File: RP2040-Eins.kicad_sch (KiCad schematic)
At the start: 55 parts, among them J1 Barrel_Jack_Switch, J10 USB_C_Receptacle_USB2.0, J2 CONN_I, J3 CONN_A, J4 CONN_P, J5 CONN_X, J7 CONN_JTAG, J8 CONN_D1, J9 CONN_D2, Q1 AO3401A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

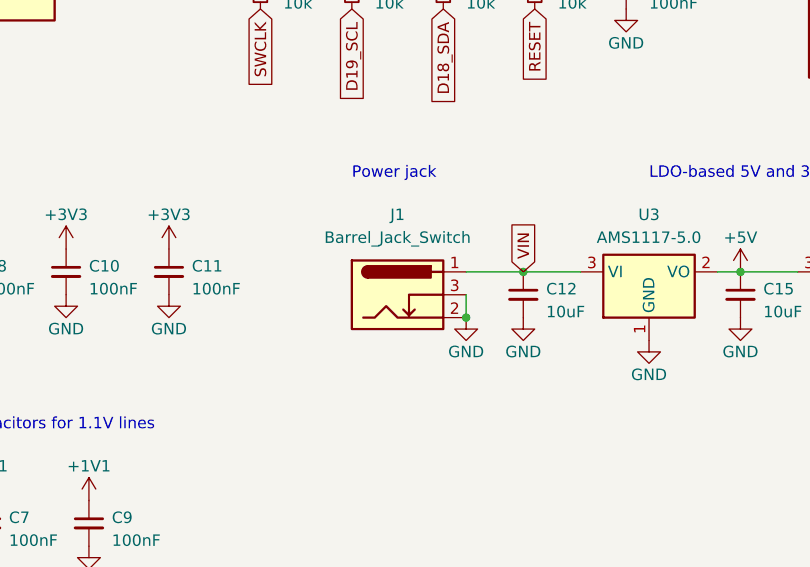
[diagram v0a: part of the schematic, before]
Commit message: Added polarity reversion protection diode
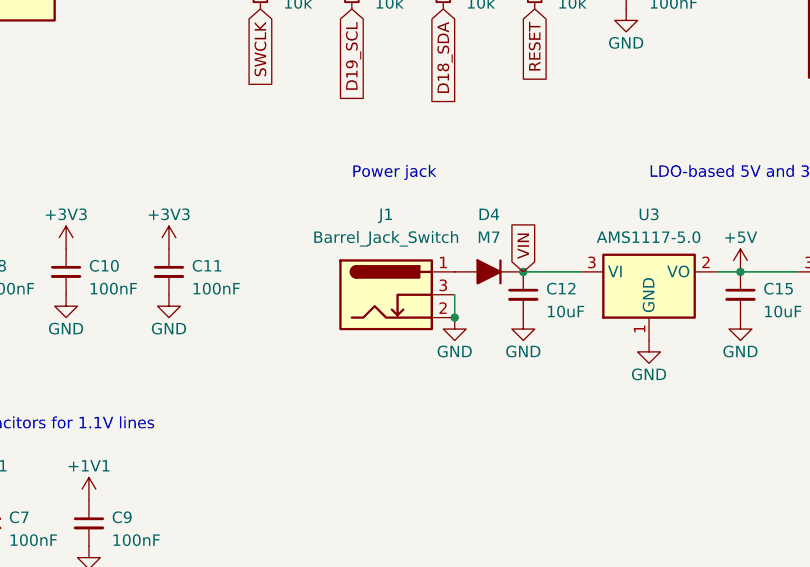
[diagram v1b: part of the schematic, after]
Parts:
- added D4: M7, PCM_4ms_Diode:D_DO-214AC_SMA, symbol PCM_Diode_AKL:M7
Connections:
- net VIN: now also D4.1 (K); no longer J1.1
- new net: D4.2 (A), J1.1
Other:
- moved on the sheet: J1
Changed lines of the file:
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@@
   (junction (at 262.89 146.05) (diameter 0) (color 0 0 0 0)
   )
+  (junction (at 207.01 151.13) (diameter 0) (color 0 0 0 0)
+  )
   (junction (at 86.36 177.8) (diameter 0) (color 0 0 0 0)
   )
@@
   (junction (at 90.17 92.71) (diameter 0) (color 0 0 0 0)
   )
-  (junction (at 208.28 151.13) (diameter 0) (color 0 0 0 0)
-  )
   (junction (at 135.89 30.48) (diameter 0) (color 0 0 0 0)
   )
@@
   (junction (at 238.76 146.05) (diameter 0) (color 0 0 0 0)
   )
-  (junction (at 49.53 96.52) (diameter 0) (color 0 0 0 0)
-  )
   (junction (at 214.63 146.05) (diameter 0) (color 0 0 0 0)
   )
+  (junction (at 49.53 96.52) (diameter 0) (color 0 0 0 0)
+  )
   (junction (at 256.54 127) (diameter 0) (color 0 0 0 0)
   )
@@
     (stroke (width 0) (type default))
   )
-  (wire (pts (xy 208.28 146.05) (xy 214.63 146.05))
-    (stroke (width 0) (type default))
-  )
   (wire (pts (xy 80.01 66.04) (xy 80.01 71.12))
     (stroke (width 0) (type default))
@@
     (stroke (width 0) (type default))
   )
+  (wire (pts (xy 207.01 148.59) (xy 207.01 151.13))
+    (stroke (width 0) (type default))
+  )
   (wire (pts (xy 143.51 30.48) (xy 146.05 30.48))
     (stroke (width 0) (type default))
@@
     (stroke (width 0) (type default))
   )
-  (wire (pts (xy 208.28 148.59) (xy 208.28 151.13))
-    (stroke (width 0) (type default))
-  )
   (wire (pts (xy 90.17 68.58) (xy 90.17 71.12))
     (stroke (width 0) (type default))
@@
     )
   )
-  (symbol (lib_id "power:GND") (at 208.28 151.13 0) (unit 1)
+  (symbol (lib_id "power:GND") (at 207.01 151.13 0) (unit 1)
     (in_bom yes) (on_board yes) (dnp no)
-    (property "Reference" "#PWR058" (at 208.28 157.48 0)
+    (property "Reference" "#PWR058" (at 207.01 157.48 0)
       (effects (font (size 1.27 1.27)) hide)
     )
-    (property "Value" "GND" (at 208.28 154.94 0)
+    (property "Value" "GND" (at 207.01 154.94 0)
       (effects (font (size 1.27 1.27)))
     )
-    (property "Footprint" "" (at 208.28 151.13 0)
+    (property "Footprint" "" (at 207.01 151.13 0)
       (effects (font (size 1.27 1.27)) hide)
     )
-    (property "Datasheet" "" (at 208.28 151.13 0)
+    (property "Datasheet" "" (at 207.01 151.13 0)
       (effects (font (size 1.27 1.27)) hide)
     )
@@
     )
   )
+  (symbol (lib_id "PCM_Diode_AKL:M7") (at 210.82 146.05 0) (unit 1)
+    (in_bom yes) (on_board yes) (dnp no) (fields_autoplaced)
+    (property "Reference" "D4" (at 210.82 139.7 0)
+      (effects (font (size 1.27 1.27)))
+    )
+    (property "Value" "M7" (at 210.82 142.24 0)
+      (effects (font (size 1.27 1.27)))
+    )
+    (property "Footprint" "PCM_4ms_Diode:D_DO-214AC_SMA" (at 210.82 146.05 0)
+      (effects (font (size 1.27 1.27)) hide)
+    )
+    (property "Datasheet" "https://www.tme.eu/Document/0550e9bf27627c5cdfb653945cb570ca/m1-m7.pdf" (at 210.82 146.05 0)
+      (effects (font (size 1.27 1.27)) hide)
+    )
+    (pin "1")
+    (pin "2")
+    (instances
+      (project "RP2040-Eins"
+        (path "/9a38a81c-7302-494f-9784-2ab4342a0a1d"
+          (reference "D4") (unit 1)
+        )
+      )
+    )
+  )
   (symbol (lib_id "Device:C_Small") (at 238.76 148.59 0) (unit 1)
     (in_bom yes) (on_board yes) (dnp no) (fields_autoplaced)
@@
     )
   )
-  (symbol (lib_id "Connector:Barrel_Jack_Switch") (at 200.66 148.59 0) (unit 1)
+  (symbol (lib_id "Connector:Barrel_Jack_Switch") (at 199.39 148.59 0) (unit 1)
     (in_bom yes) (on_board yes) (dnp no) (fields_autoplaced)
-    (property "Reference" "J1" (at 200.66 139.7 0)
+    (property "Reference" "J1" (at 199.39 139.7 0)
       (effects (font (size 1.27 1.27)))
     )
-    (property "Value" "Barrel_Jack_Switch" (at 200.66 142.24 0)
+    (property "Value" "Barrel_Jack_Switch" (at 199.39 142.24 0)
       (effects (font (size 1.27 1.27)))
     )
-    (property "Footprint" "Connector_BarrelJack:BarrelJack_Horizontal" (at 201.93 149.606 0)
+    (property "Footprint" "Connector_BarrelJack:BarrelJack_Horizontal" (at 200.66 149.606 0)
       (effects (font (size 1.27 1.27)) hide)
     )
-    (property "Datasheet" "~" (at 201.93 149.606 0)
+    (property "Datasheet" "~" (at 200.66 149.606 0)
       (effects (font (size 1.27 1.27)) hide)
     )

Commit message: Moved stuff around
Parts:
- added C22: 100nF, Capacitor_SMD:C_0402_1005Metric, symbol Device:C_Small
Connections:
- net +1V1: now also C22.1
- net GND: now also C22.2
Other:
- moved on the sheet: C17, C18, C5, C7, C9

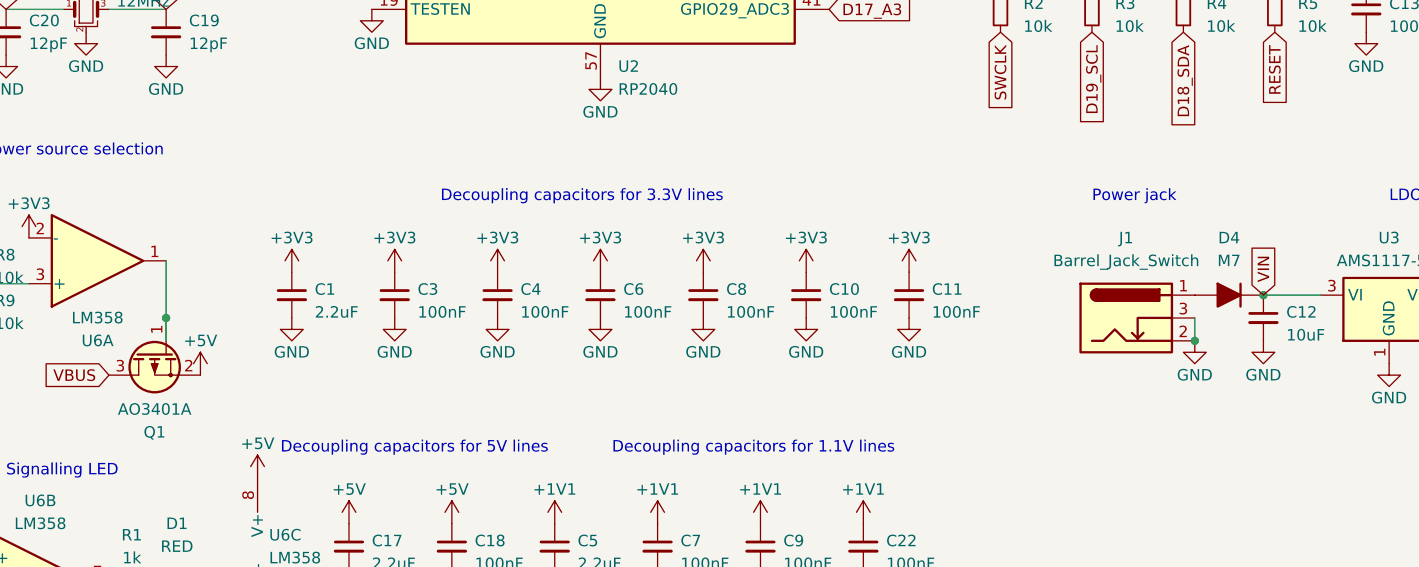
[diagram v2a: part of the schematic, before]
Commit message: Put schottky diode instead of normal one.
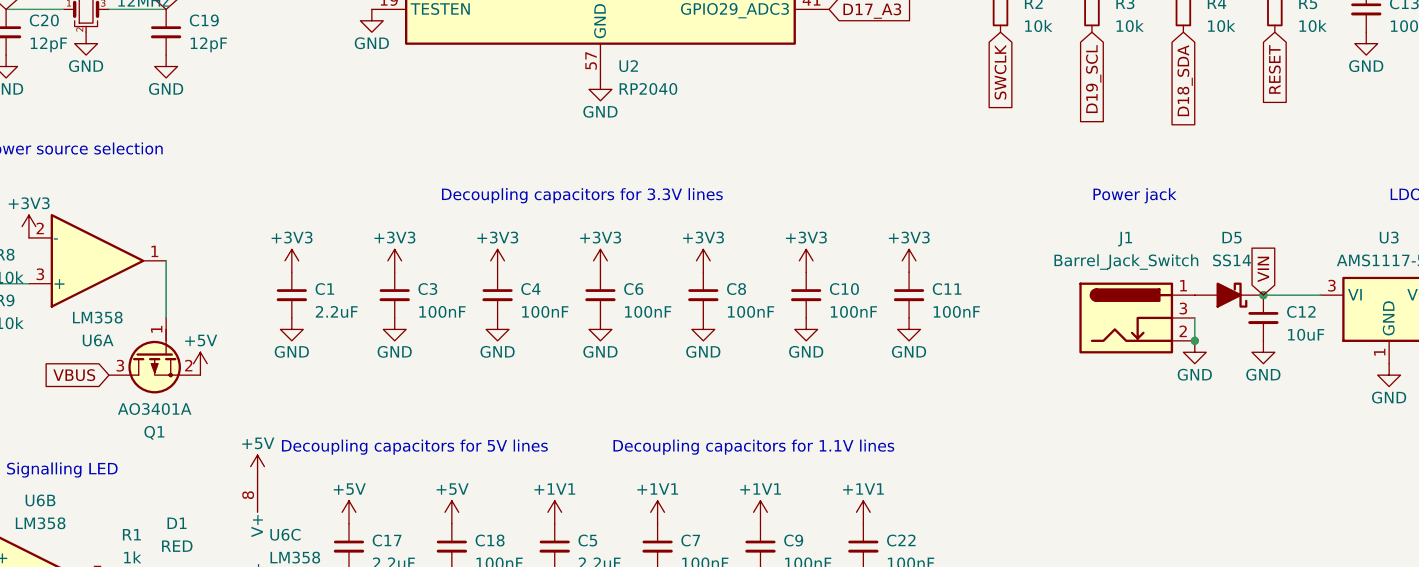
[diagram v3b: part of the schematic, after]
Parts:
- removed D4: M7, PCM_4ms_Diode:D_DO-214AC_SMA, symbol PCM_Diode_AKL:M7
- added D5: SS14, PCM_4ms_Diode:D_DO-214AC_SMA, symbol PCM_Diode_Schottky_AKL:SS14
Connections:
- net VIN: now also D5.1 (K)
- net at J1.1: now also D5.2 (A)
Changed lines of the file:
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@@
   (junction (at 207.01 151.13) (diameter 0) (color 0 0 0 0)
   )
-  (junction (at 86.36 177.8) (diameter 0) (color 0 0 0 0)
+  (junction (at 214.63 146.05) (diameter 0) (color 0 0 0 0)
   )
-  (junction (at 92.71 148.59) (diameter 0) (color 0 0 0 0)
+  (junction (at 86.36 177.8) (diameter 0) (color 0 0 0 0)
   )
   (junction (at 148.59 30.48) (diameter 0) (color 0 0 0 0)
@@
   (junction (at 238.76 146.05) (diameter 0) (color 0 0 0 0)
   )
-  (junction (at 214.63 146.05) (diameter 0) (color 0 0 0 0)
-  )
   (junction (at 49.53 96.52) (diameter 0) (color 0 0 0 0)
   )
@@
     (stroke (width 0) (type default))
   )
-  (wire (pts (xy 92.71 148.59) (xy 92.71 151.13))
-    (stroke (width 0) (type default))
-  )
   (wire (pts (xy 135.89 30.48) (xy 138.43 30.48))
     (stroke (width 0) (type default))
@@
     (stroke (width 0) (type default))
   )
-  (wire (pts (xy 203.2 53.34) (xy 203.2 55.88))
+  (wire (pts (xy 92.71 142.24) (xy 92.71 148.59))
     (stroke (width 0) (type default))
   )
-  (wire (pts (xy 260.35 146.05) (xy 262.89 146.05))
+  (wire (pts (xy 203.2 53.34) (xy 203.2 55.88))
     (stroke (width 0) (type default))
   )
-  (wire (pts (xy 92.71 142.24) (xy 92.71 148.59))
+  (wire (pts (xy 260.35 146.05) (xy 262.89 146.05))
     (stroke (width 0) (type default))
   )
@@
     )
   )
+  (symbol (lib_id "PCM_Diode_Schottky_AKL:SS14") (at 210.82 146.05 0) (unit 1)
+    (in_bom yes) (on_board yes) (dnp no) (fields_autoplaced)
+    (property "Reference" "D5" (at 211.1375 139.7 0)
+      (effects (font (size 1.27 1.27)))
+    )
+    (property "Value" "SS14" (at 211.1375 142.24 0)
+      (effects (font (size 1.27 1.27)))
+    )
+    (property "Footprint" "PCM_4ms_Diode:D_DO-214AC_SMA" (at 210.82 146.05 0)
+      (effects (font (size 1.27 1.27)) hide)
+    )
+    (property "Datasheet" "https://www.tme.eu/Document/39e1c2d2c354f63d74e9a2edb2156b4b/SS14-E3_61T.pdf" (at 210.82 146.05 0)
+      (effects (font (size 1.27 1.27)) hide)
+    )
+    (pin "1")
+    (pin "2")
+    (instances
+      (project "RP2040-Eins"
+        (path "/9a38a81c-7302-494f-9784-2ab4342a0a1d"
+          (reference "D5") (unit 1)
+        )
+      )
+    )
+  )
   (symbol (lib_id "Amplifier_Operational:LM358") (at 85.09 142.24 0) (mirror x) (unit 1)
     (in_bom yes) (on_board yes) (dnp no)
@@
         )
       )
-    )
-  )
-  (symbol (lib_id "PCM_Diode_AKL:M7") (at 210.82 146.05 0) (unit 1)
-    (in_bom yes) (on_board yes) (dnp no) (fields_autoplaced)
-    (property "Reference" "D4" (at 210.82 139.7 0)
-      (effects (font (size 1.27 1.27)))
-    )
-    (property "Value" "M7" (at 210.82 142.24 0)
-      (effects (font (size 1.27 1.27)))
-    )
-    (property "Footprint" "PCM_4ms_Diode:D_DO-214AC_SMA" (at 210.82 146.05 0)
-      (effects (font (size 1.27 1.27)) hide)
-    )
-    (property "Datasheet" "https://www.tme.eu/Document/0550e9bf27627c5cdfb653945cb570ca/m1-m7.pdf" (at 210.82 146.05 0)
-      (effects (font (size 1.27 1.27)) hide)
-    )
-    (pin "1")
-    (pin "2")
-    (instances
-      (project "RP2040-Eins"
-        (path "/9a38a81c-7302-494f-9784-2ab4342a0a1d"
-          (reference "D4") (unit 1)
-        )
-      )

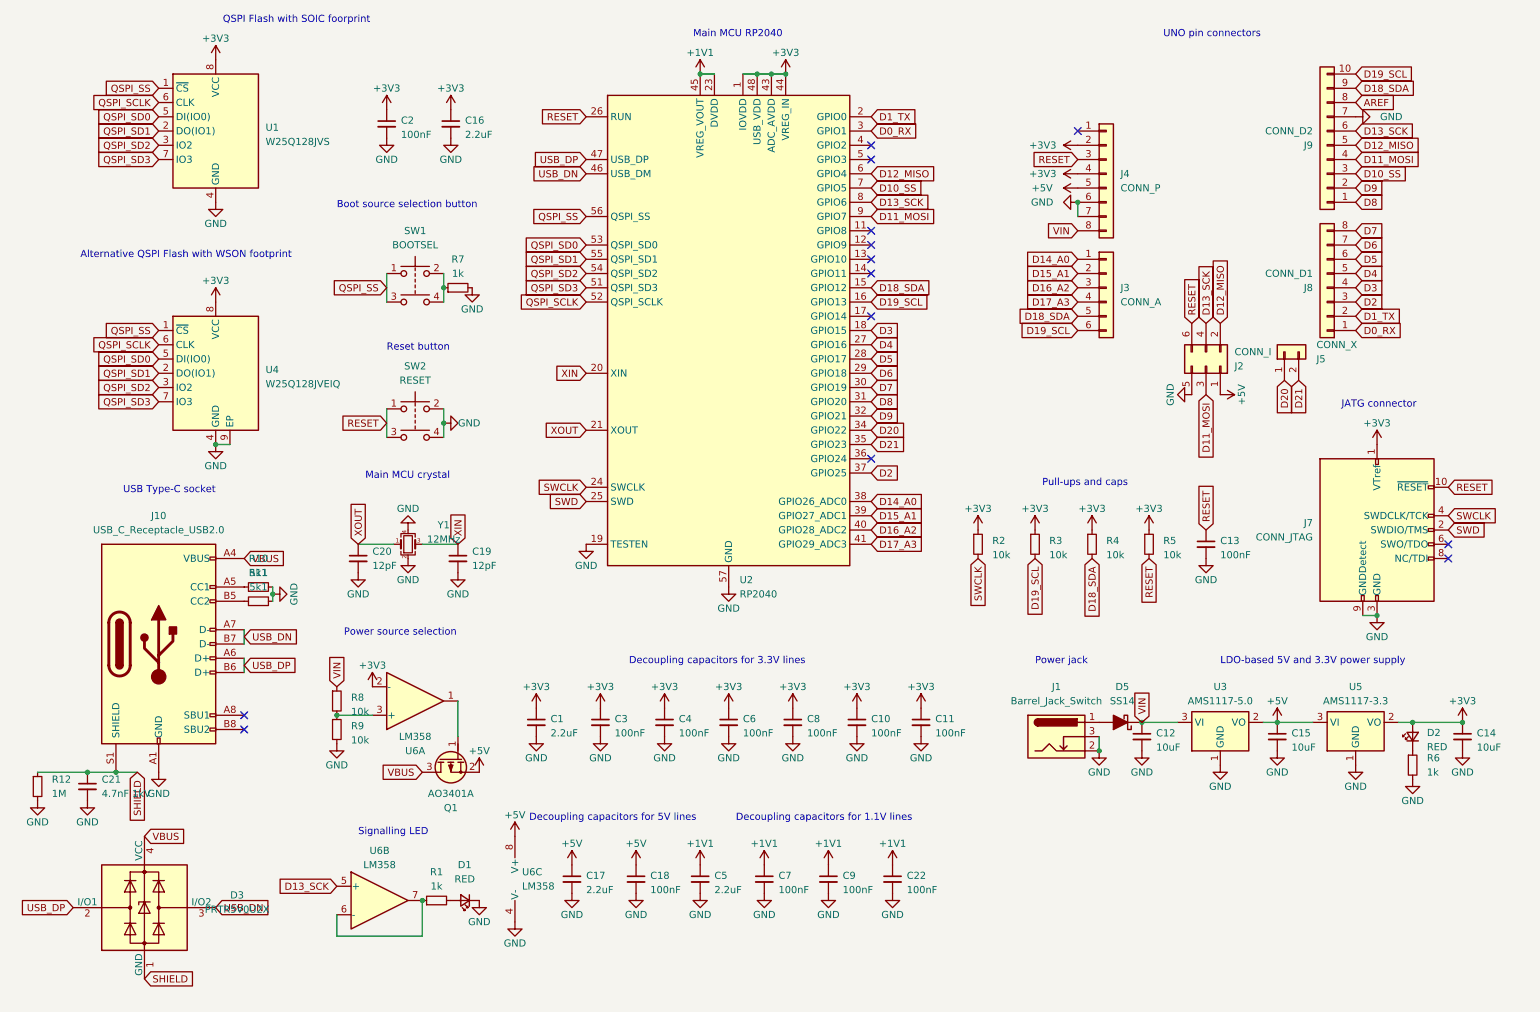
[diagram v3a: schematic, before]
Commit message: Simplified the schematics a bit
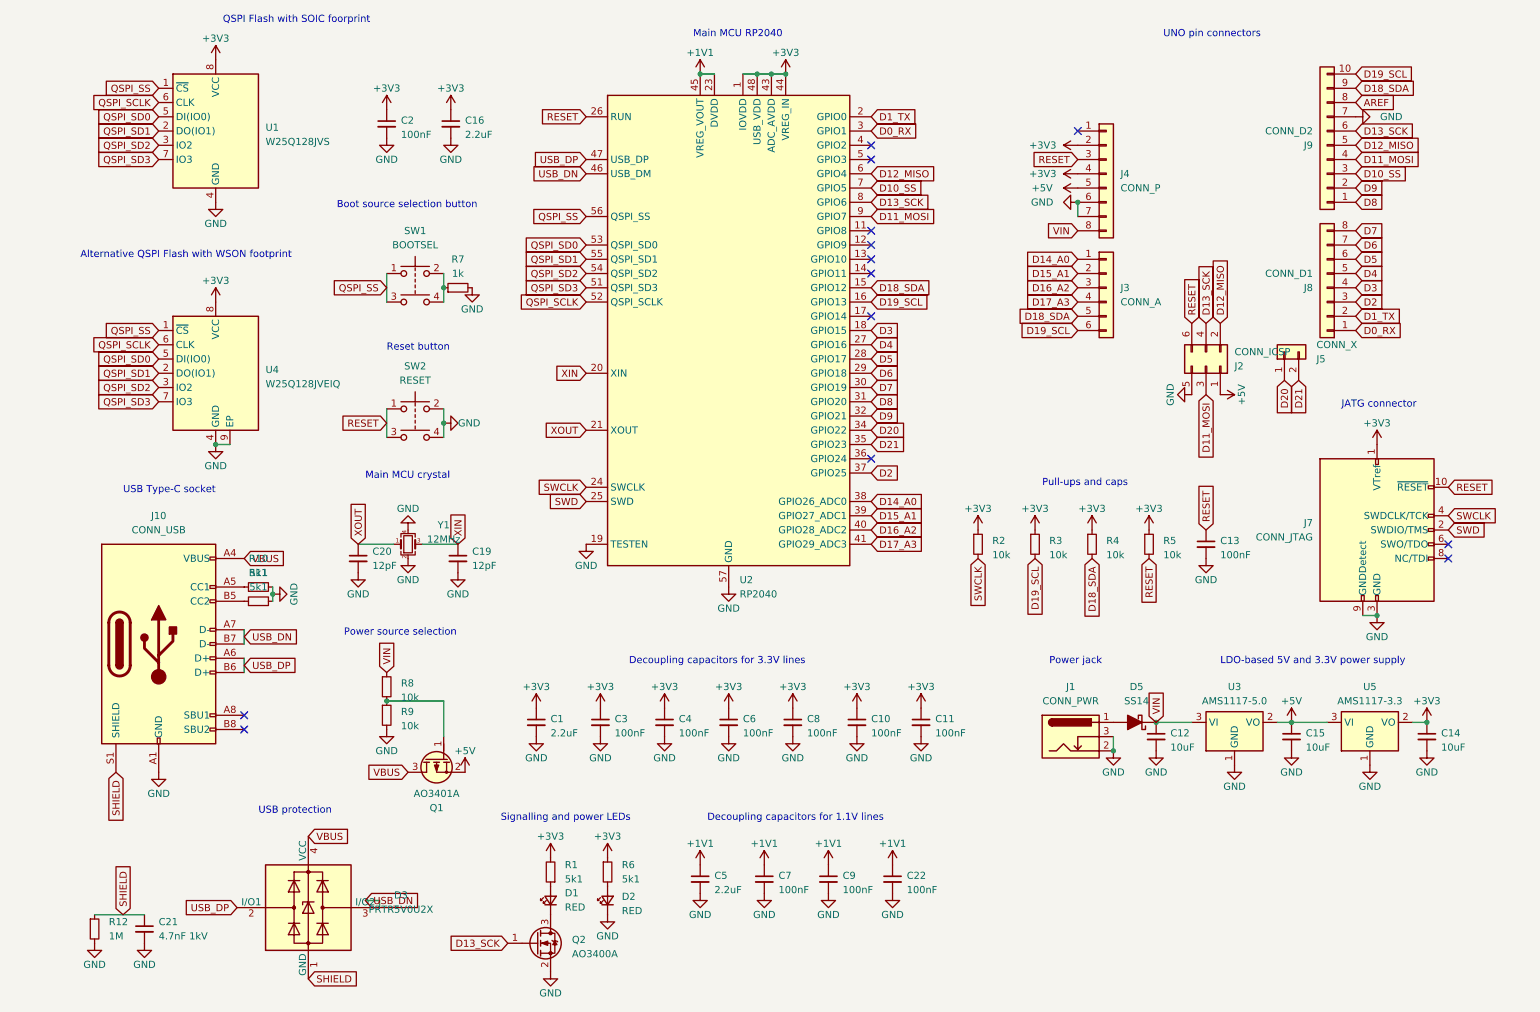
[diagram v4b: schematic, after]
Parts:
- removed C17: 2.2uF, Capacitor_SMD:C_0603_1608Metric, symbol Device:C_Small
- removed C18: 100nF, Capacitor_SMD:C_0402_1005Metric, symbol Device:C_Small
- removed U6: LM358, Package_SO:SOIC-8_3.9x4.9mm_P1.27mm, symbol Amplifier_Operational:LM358
- added Q2: AO3400A, Package_TO_SOT_SMD:SOT-23, symbol Transistor_FET:AO3400A
- J1: value Barrel_Jack_Switch -> CONN_PWR
- J10: value USB_C_Receptacle_USB2.0 -> CONN_USB
- J2: value CONN_I -> CONN_ICSP
- R1, R6: value 1k -> 5k1
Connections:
- net +3V3: now also R1.2, R6.1; no longer D2.2 (A)
- net D13_SCK: now also Q2.1 (G)
- net GND: now also D2.1 (K), Q2.2 (S); no longer D1.1 (K), R6.2
- net at R1.1: now also D1.2 (A)
- net at R8.2, R9.1: now also Q1.1 (G)
- new net: D1.1 (K), Q2.3 (D)
- new net: D2.2 (A), R6.2
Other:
- note added: "Signalling and power LEDs"
- note added: "USB protection"
- note removed: "Decoupling capacitors for 5V lines"
- note removed: "Signalling LED"
- moved on the sheet: C12, C14, C15, C21, D1, D2, D3, D5, J1, Q1, R1, R12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
